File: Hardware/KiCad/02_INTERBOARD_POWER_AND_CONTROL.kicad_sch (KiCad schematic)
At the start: 0 parts

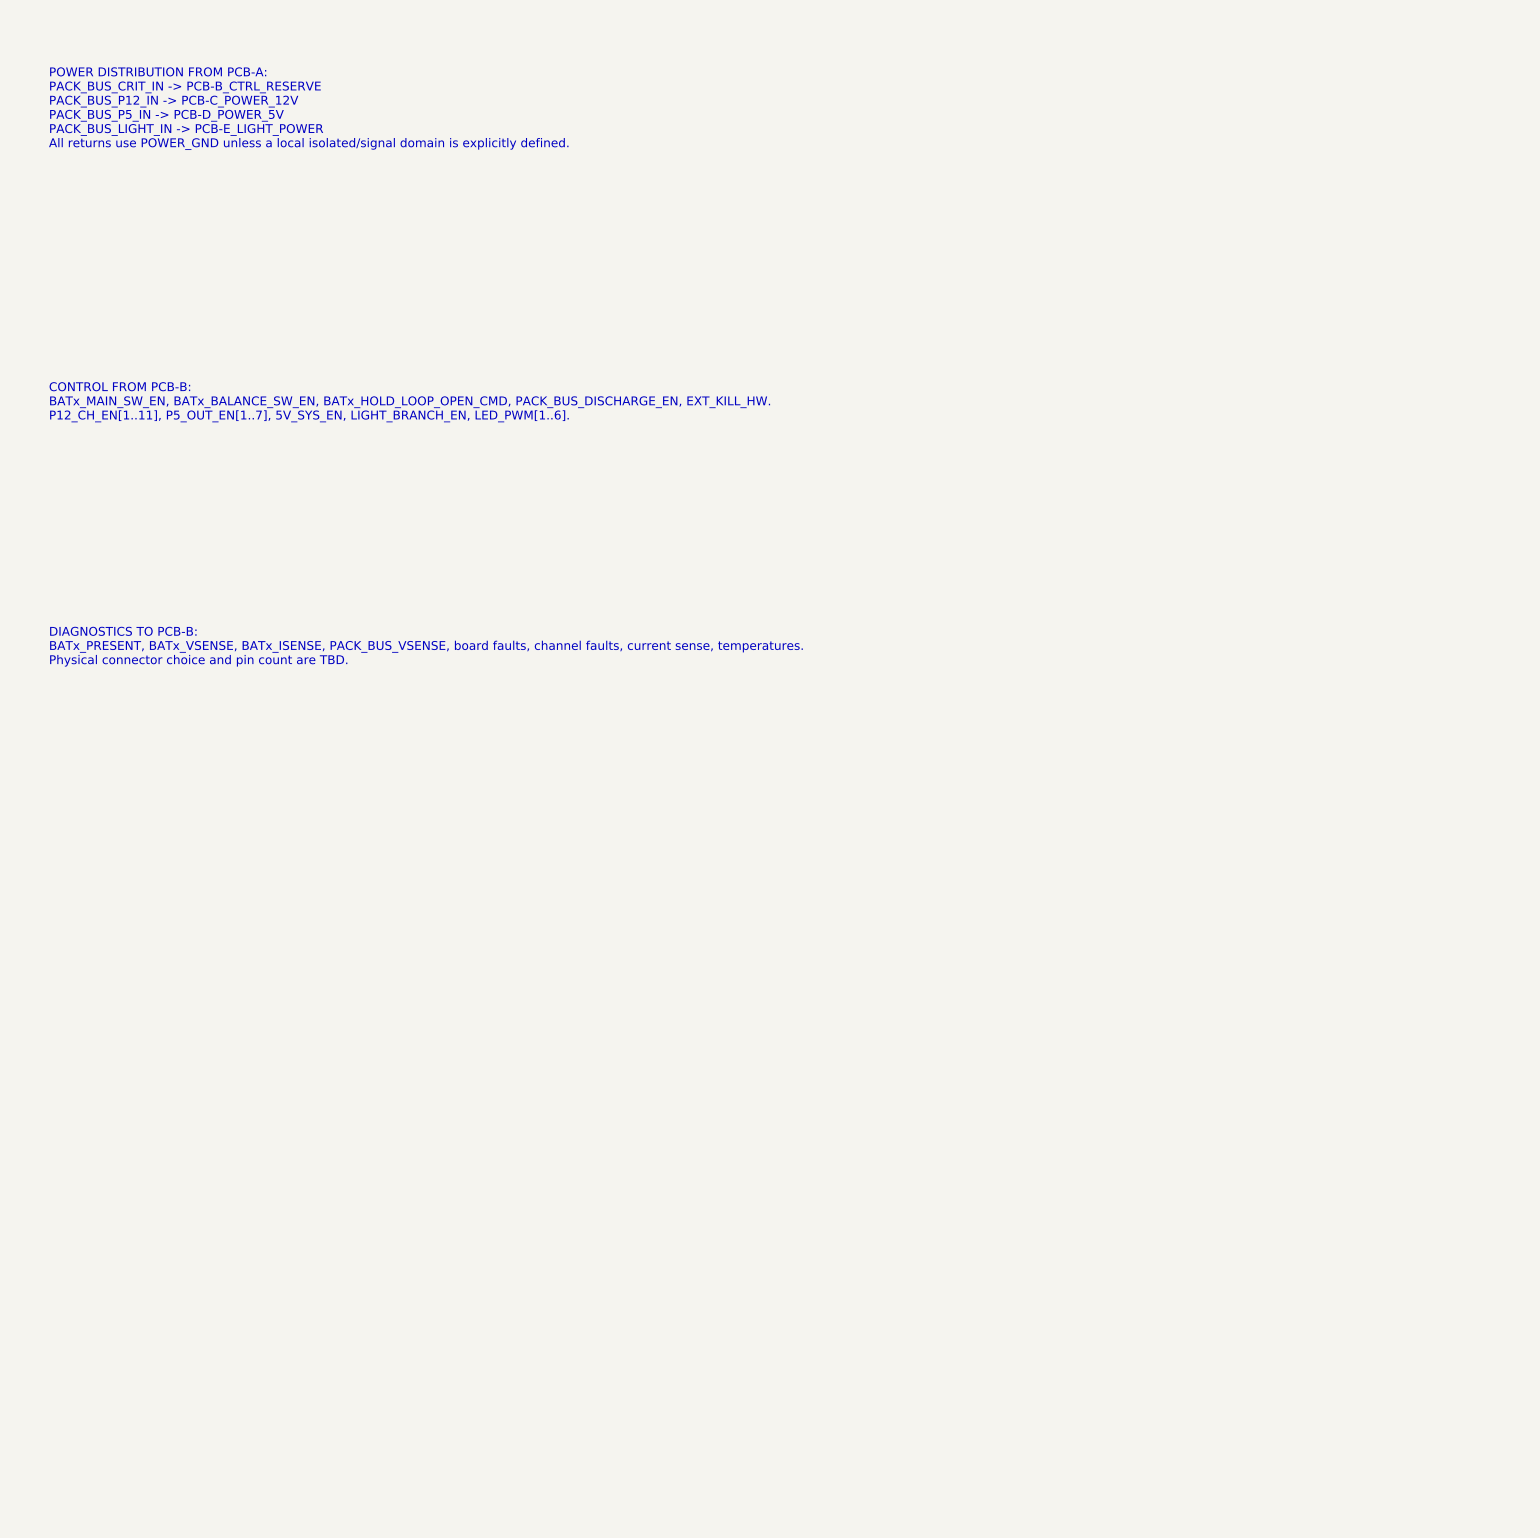
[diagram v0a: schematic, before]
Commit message: hardware: detail interboard power and control matrix
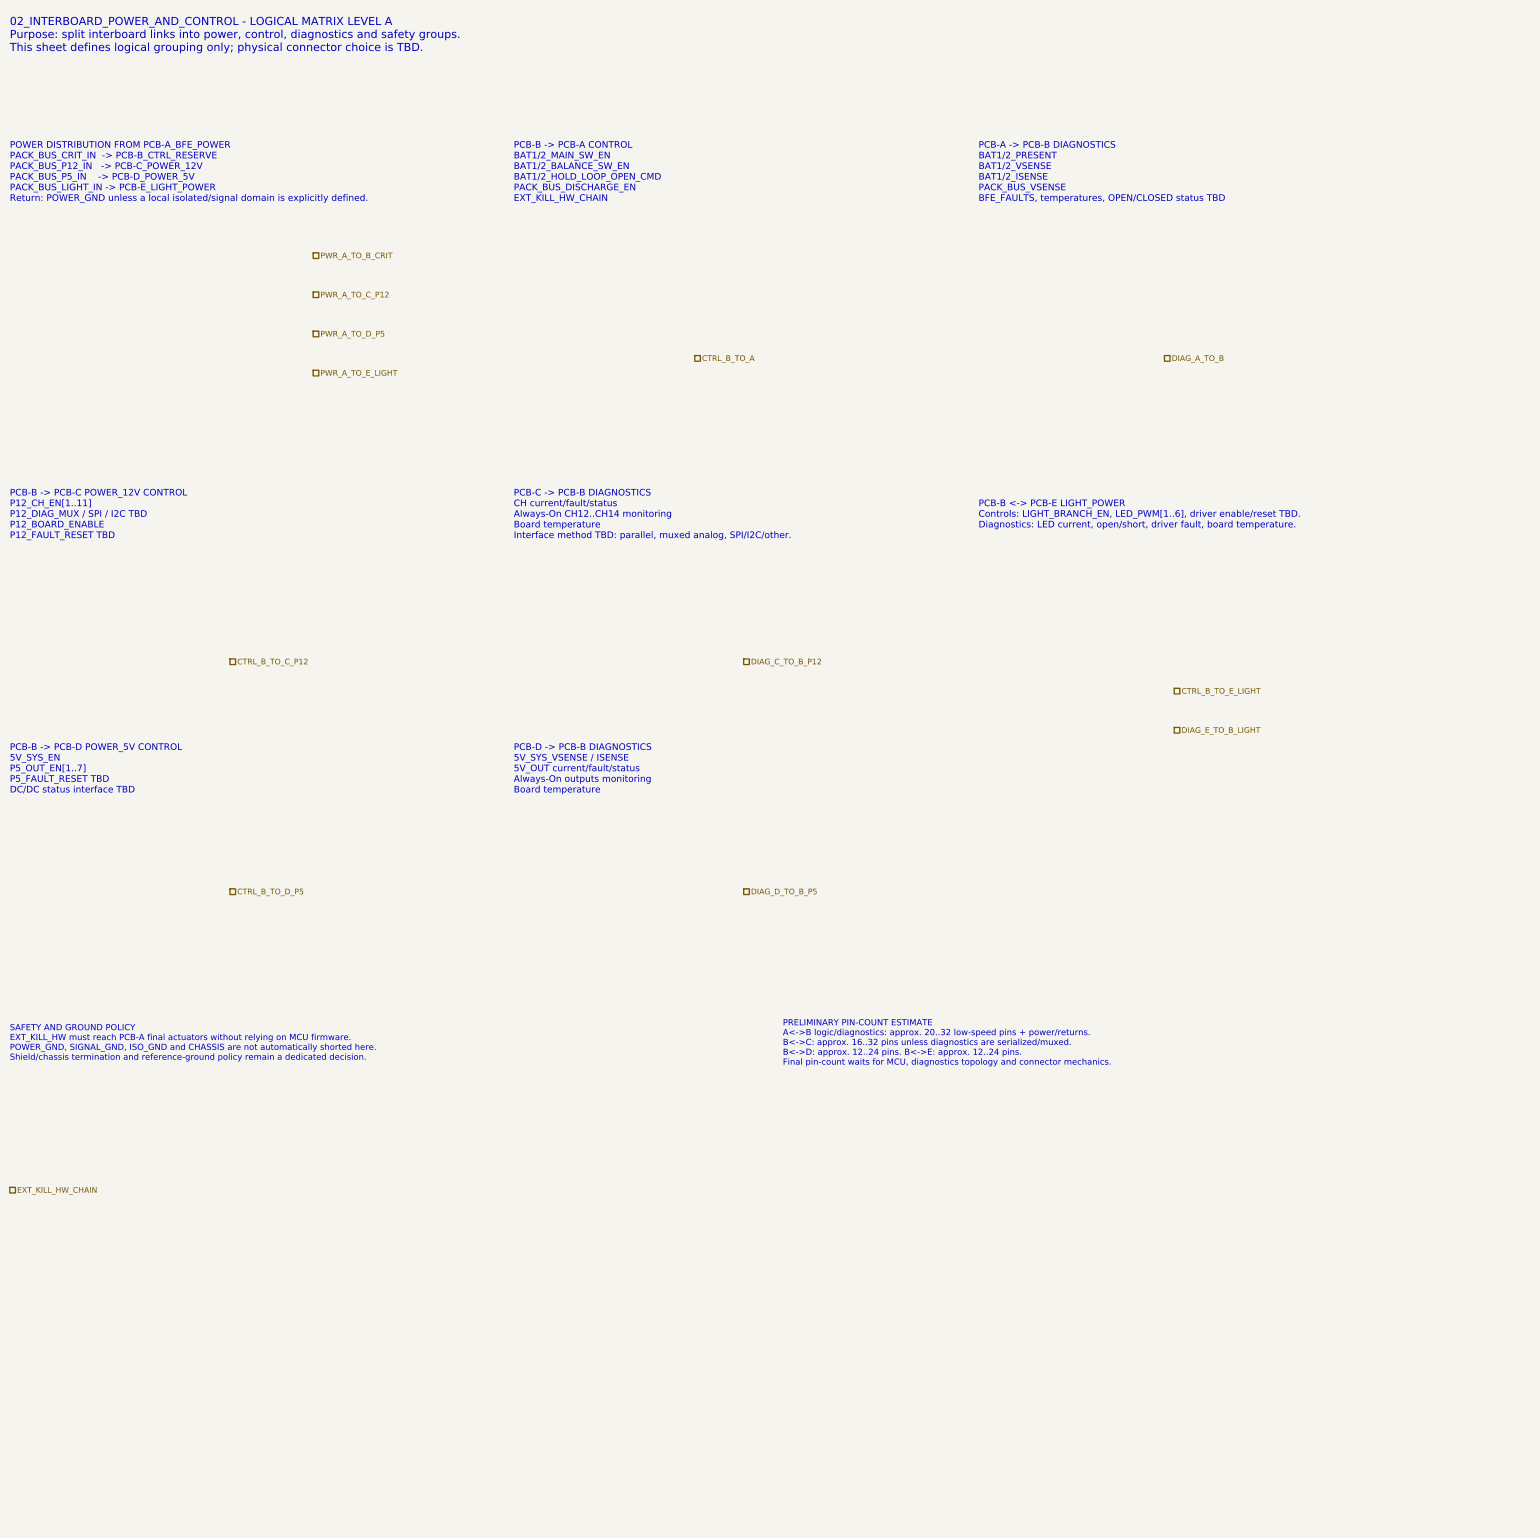
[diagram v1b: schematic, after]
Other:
- note added: "02_INTERBOARD_POWER_AND_CONTROL - LOGICAL MATRIX LEVEL A Purpose: split interboard links into power, control, diagnostics and safety groups. This sheet defines logical grouping only; physical connector choice is TBD."
- note added: "PCB-A -> PCB-B DIAGNOSTICS BAT1/2_PRESENT BAT1/2_VSENSE BAT1/2_ISENSE PACK_BUS_VSENSE BFE_FAULTS, temperatures, OPEN/CLOSED status TBD"
- note added: "PCB-B -> PCB-A CONTROL BAT1/2_MAIN_SW_EN BAT1/2_BALANCE_SW_EN BAT1/2_HOLD_LOOP_OPEN_CMD PACK_BUS_DISCHARGE_EN EXT_KILL_HW_CHAIN"
- note added: "PCB-B -> PCB-C POWER_12V CONTROL P12_CH_EN[1..11] P12_DIAG_MUX / SPI / I2C TBD P12_BOARD_ENABLE P12_FAULT_RESET TBD"
- note added: "PCB-B -> PCB-D POWER_5V CONTROL 5V_SYS_EN P5_OUT_EN[1..7] P5_FAULT_RESET TBD DC/DC status interface TBD"
- note added: "PCB-B <-> PCB-E LIGHT_POWER Controls: LIGHT_BRANCH_EN, LED_PWM[1..6], driver enable/reset TBD. Diagnostics: LED current, open/short, driver fault, board temperature."
- note added: "PCB-C -> PCB-B DIAGNOSTICS CH current/fault/status Always-On CH12..CH14 monitoring Board temperature Interface method TBD: parallel, muxed analog, SPI/I2C/other."
- note added: "PCB-D -> PCB-B DIAGNOSTICS 5V_SYS_VSENSE / ISENSE 5V_OUT current/fault/status Always-On outputs monitoring Board temperature"
- note added: "POWER DISTRIBUTION FROM PCB-A_BFE_POWER PACK_BUS_CRIT_IN -> PCB-B_CTRL_RESERVE PACK_BUS_P12_IN -> PCB-C_POWER_12V PACK_BUS_P5_IN -> PCB-D_POWER_5V PACK_BUS_LIGHT_IN -> PCB-E_LIGHT_POWER Return: POWER_GND unless a local isolated/signal domain is explicitly defined."
- note added: "PRELIMINARY PIN-COUNT ESTIMATE A<->B logic/diagnostics: approx. 20..32 low-speed pins + power/returns. B<->C: approx. 16..32 pins unless diagnostics are serialized/muxed. B<->D: approx. 12..24 pins. B<->E: approx. 12..24 pins. Final pin-count waits for MCU, diagnostics topology and connector mechanics."
- note added: "SAFETY AND GROUND POLICY EXT_KILL_HW must reach PCB-A final actuators without relying on MCU firmware. POWER_GND, SIGNAL_GND, ISO_GND and CHASSIS are not automatically shorted here. Shield/chassis termination and reference-ground policy remain a dedicated decision."
- note removed: "CONTROL FROM PCB-B: BATx_MAIN_SW_EN, BATx_BALANCE_SW_EN, BATx_HOLD_LOOP_OPEN_CMD, PACK_BUS_DISCHARGE_EN, EXT_KILL_HW. P12_CH_EN[1..11], P5_OUT_EN[1..7], 5V_SYS_EN, LIGHT_BRANCH_EN, LED_PWM[1..6]."
- note removed: "DIAGNOSTICS TO PCB-B: BATx_PRESENT, BATx_VSENSE, BATx_ISENSE, PACK_BUS_VSENSE, board faults, channel faults, current sense, temperatures. Physical connector choice and pin count are TBD."
- note removed: "POWER DISTRIBUTION FROM PCB-A: PACK_BUS_CRIT_IN -> PCB-B_CTRL_RESERVE PACK_BUS_P12_IN -> PCB-C_POWER_12V PACK_BUS_P5_IN -> PCB-D_POWER_5V PACK_BUS_LIGHT_IN -> PCB-E_LIGHT_POWER All returns use POWER_GND unless a local isolated/signal domain is explicitly defined."
- company: (none) -> Gonoboben/plataVM

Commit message: hardware: align system interboard matrix to V1.6 CAN-FD policy
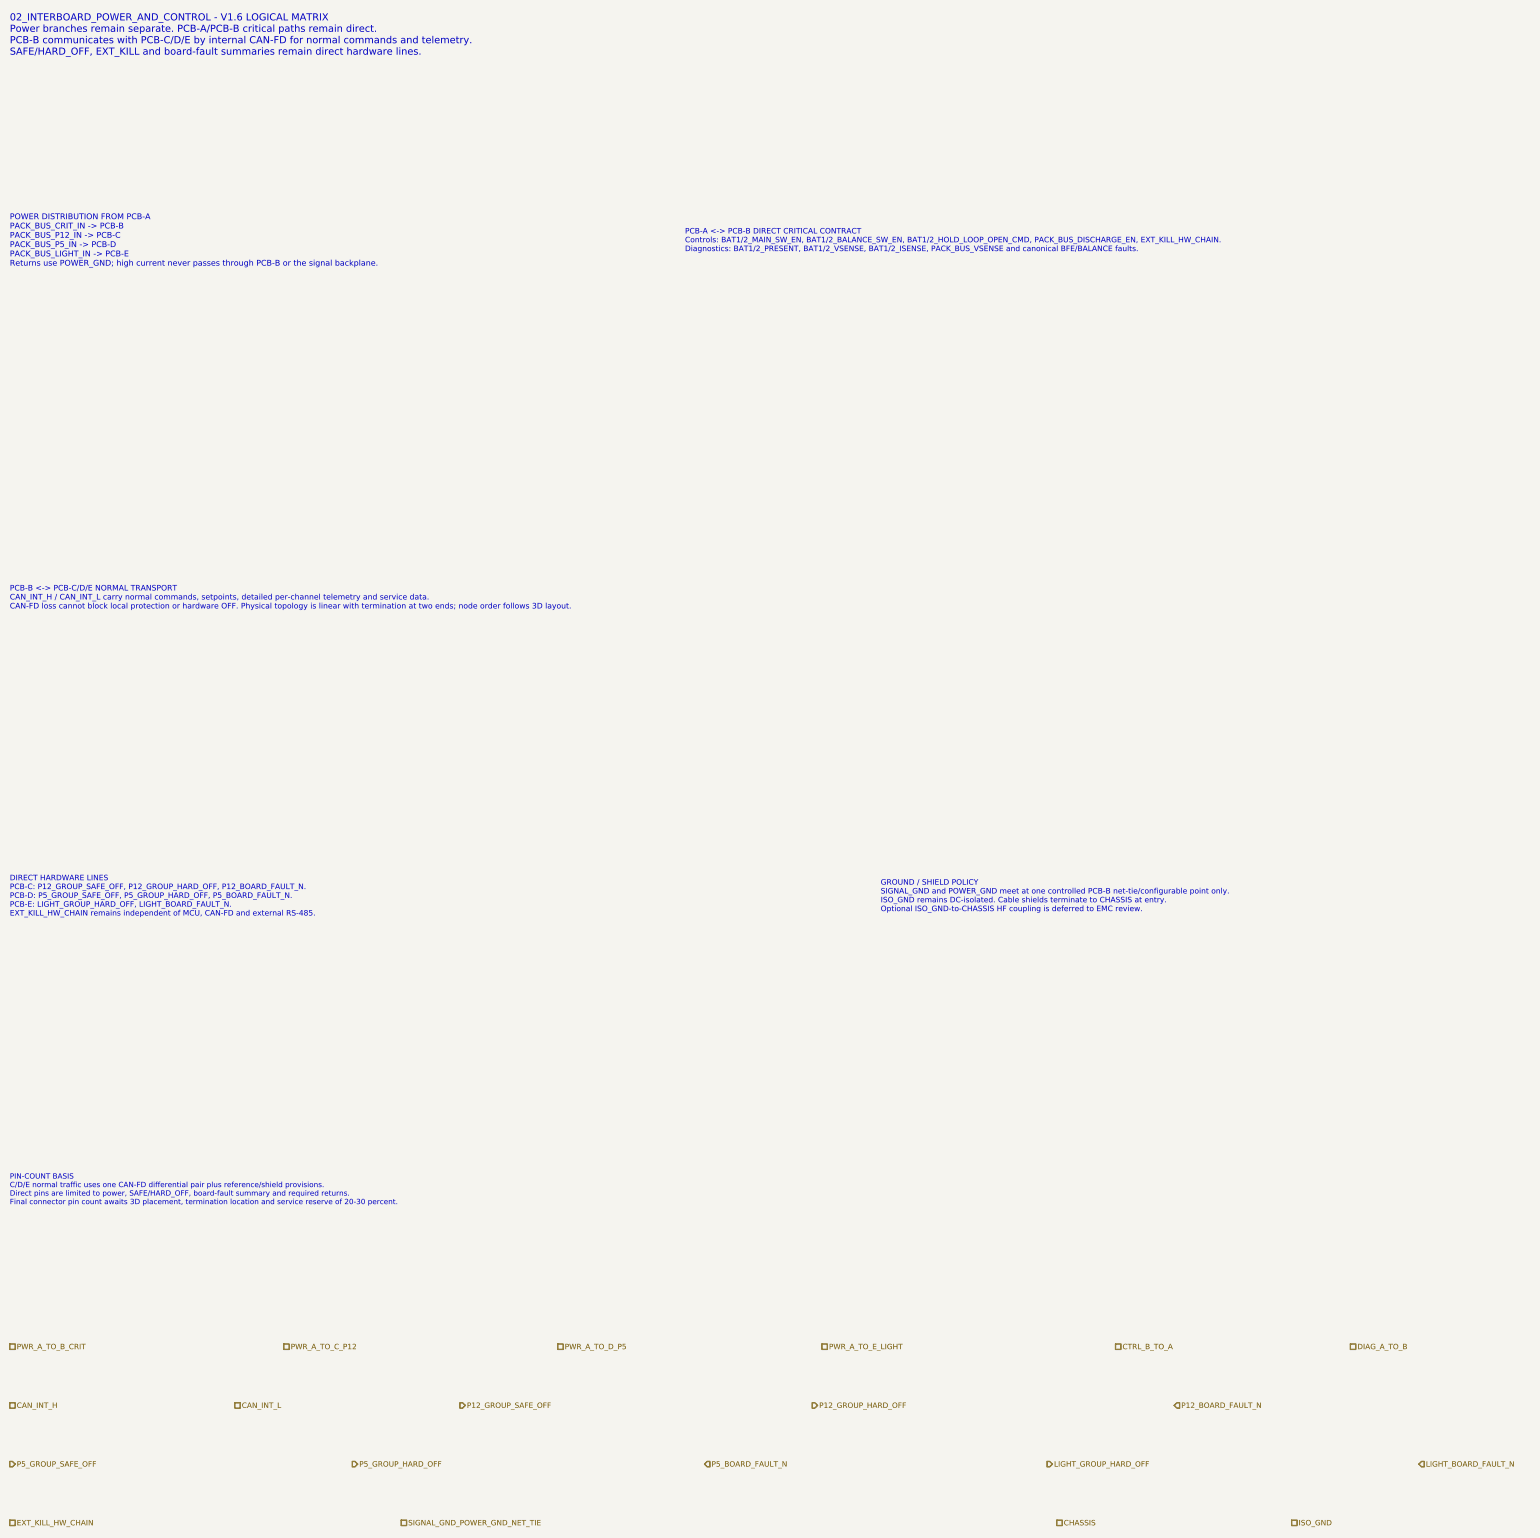
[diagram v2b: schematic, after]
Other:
- note added: "02_INTERBOARD_POWER_AND_CONTROL - V1.6 LOGICAL MATRIX Power branches remain separate. PCB-A/PCB-B critical paths remain direct. PCB-B communicates with PCB-C/D/E by internal CAN-FD for normal commands and telemetry. SAFE/HARD_OFF, EXT_KILL and board-fault summaries remain direct hardware lines."
- note added: "DIRECT HARDWARE LINES PCB-C: P12_GROUP_SAFE_OFF, P12_GROUP_HARD_OFF, P12_BOARD_FAULT_N. PCB-D: P5_GROUP_SAFE_OFF, P5_GROUP_HARD_OFF, P5_BOARD_FAULT_N. PCB-E: LIGHT_GROUP_HARD_OFF, LIGHT_BOARD_FAULT_N. EXT_KILL_HW_CHAIN remains independent of MCU, CAN-FD and external RS-485."
- note added: "GROUND / SHIELD POLICY SIGNAL_GND and POWER_GND meet at one controlled PCB-B net-tie/configurable point only. ISO_GND remains DC-isolated. Cable shields terminate to CHASSIS at entry. Optional ISO_GND-to-CHASSIS HF coupling is deferred to EMC review."
- note added: "PCB-A <-> PCB-B DIRECT CRITICAL CONTRACT Controls: BAT1/2_MAIN_SW_EN, BAT1/2_BALANCE_SW_EN, BAT1/2_HOLD_LOOP_OPEN_CMD, PACK_BUS_DISCHARGE_EN, EXT_KILL_HW_CHAIN. Diagnostics: BAT1/2_PRESENT, BAT1/2_VSENSE, BAT1/2_ISENSE, PACK_BUS_VSENSE and canonical BFE/BALANCE faults."
- note added: "PCB-B <-> PCB-C/D/E NORMAL TRANSPORT CAN_INT_H / CAN_INT_L carry normal commands, setpoints, detailed per-channel telemetry and service data. CAN-FD loss cannot block local protection or hardware OFF. Physical topology is linear with termination at two ends; node order follows 3D layout."
- note added: "PIN-COUNT BASIS C/D/E normal traffic uses one CAN-FD differential pair plus reference/shield provisions. Direct pins are limited to power, SAFE/HARD_OFF, board-fault summary and required returns. Final connector pin count awaits 3D placement, termination location and service reserve of 20-30 percent."
- note added: "POWER DISTRIBUTION FROM PCB-A PACK_BUS_CRIT_IN -> PCB-B PACK_BUS_P12_IN -> PCB-C PACK_BUS_P5_IN -> PCB-D PACK_BUS_LIGHT_IN -> PCB-E Returns use POWER_GND; high current never passes through PCB-B or the signal backplane."
- note removed: "02_INTERBOARD_POWER_AND_CONTROL - LOGICAL MATRIX LEVEL A Purpose: split interboard links into power, control, diagnostics and safety groups. This sheet defines logical grouping only; physical connector choice is TBD."
- note removed: "PCB-A -> PCB-B DIAGNOSTICS BAT1/2_PRESENT BAT1/2_VSENSE BAT1/2_ISENSE PACK_BUS_VSENSE BFE_FAULTS, temperatures, OPEN/CLOSED status TBD"
- note removed: "PCB-B -> PCB-A CONTROL BAT1/2_MAIN_SW_EN BAT1/2_BALANCE_SW_EN BAT1/2_HOLD_LOOP_OPEN_CMD PACK_BUS_DISCHARGE_EN EXT_KILL_HW_CHAIN"
- note removed: "PCB-B -> PCB-C POWER_12V CONTROL P12_CH_EN[1..11] P12_DIAG_MUX / SPI / I2C TBD P12_BOARD_ENABLE P12_FAULT_RESET TBD"
- note removed: "PCB-B -> PCB-D POWER_5V CONTROL 5V_SYS_EN P5_OUT_EN[1..7] P5_FAULT_RESET TBD DC/DC status interface TBD"
- note removed: "PCB-B <-> PCB-E LIGHT_POWER Controls: LIGHT_BRANCH_EN, LED_PWM[1..6], driver enable/reset TBD. Diagnostics: LED current, open/short, driver fault, board temperature."
- note removed: "PCB-C -> PCB-B DIAGNOSTICS CH current/fault/status Always-On CH12..CH14 monitoring Board temperature Interface method TBD: parallel, muxed analog, SPI/I2C/other."
- note removed: "PCB-D -> PCB-B DIAGNOSTICS 5V_SYS_VSENSE / ISENSE 5V_OUT current/fault/status Always-On outputs monitoring Board temperature"
- note removed: "POWER DISTRIBUTION FROM PCB-A_BFE_POWER PACK_BUS_CRIT_IN -> PCB-B_CTRL_RESERVE PACK_BUS_P12_IN -> PCB-C_POWER_12V PACK_BUS_P5_IN -> PCB-D_POWER_5V PACK_BUS_LIGHT_IN -> PCB-E_LIGHT_POWER Return: POWER_GND unless a local isolated/signal domain is explicitly defined."
- note removed: "PRELIMINARY PIN-COUNT ESTIMATE A<->B logic/diagnostics: approx. 20..32 low-speed pins + power/returns. B<->C: approx. 16..32 pins unless diagnostics are serialized/muxed. B<->D: approx. 12..24 pins. B<->E: approx. 12..24 pins. Final pin-count waits for MCU, diagnostics topology and connector mechanics."
- note removed: "SAFETY AND GROUND POLICY EXT_KILL_HW must reach PCB-A final actuators without relying on MCU firmware. POWER_GND, SIGNAL_GND, ISO_GND and CHASSIS are not automatically shorted here. Shield/chassis termination and reference-ground policy remain a dedicated decision."
